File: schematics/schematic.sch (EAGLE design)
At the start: 22 parts, among them U1 TSR_1-2450

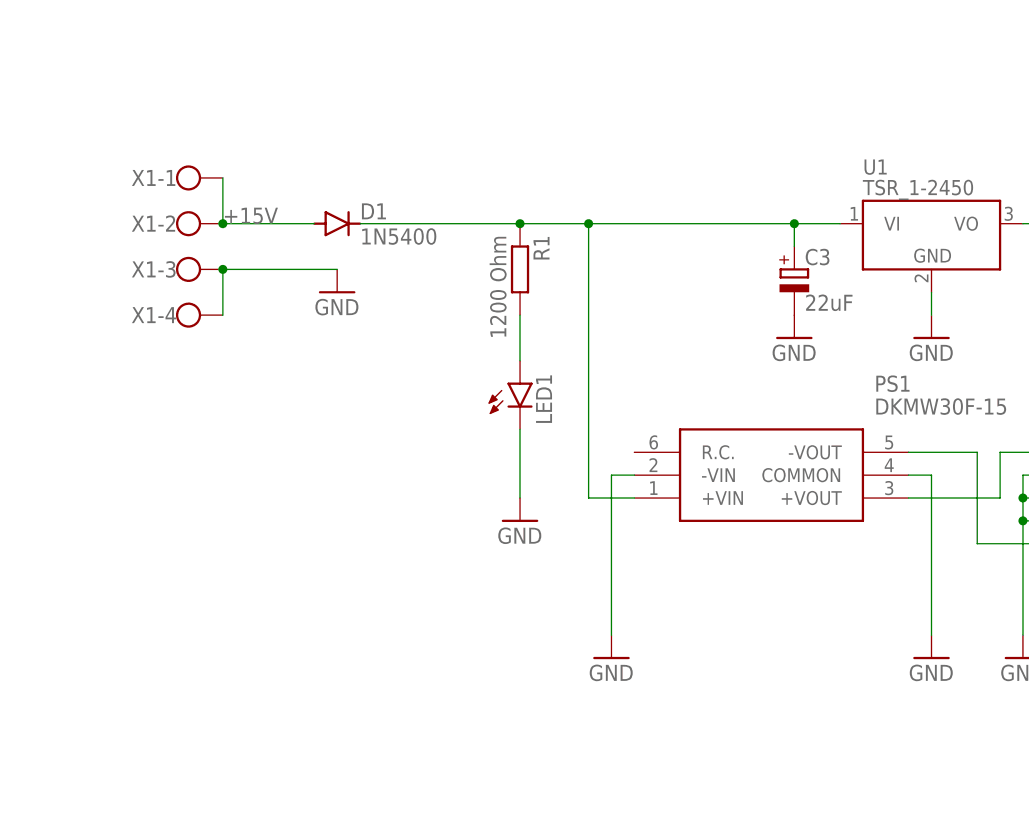
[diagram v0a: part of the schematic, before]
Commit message: added 2 crc groups
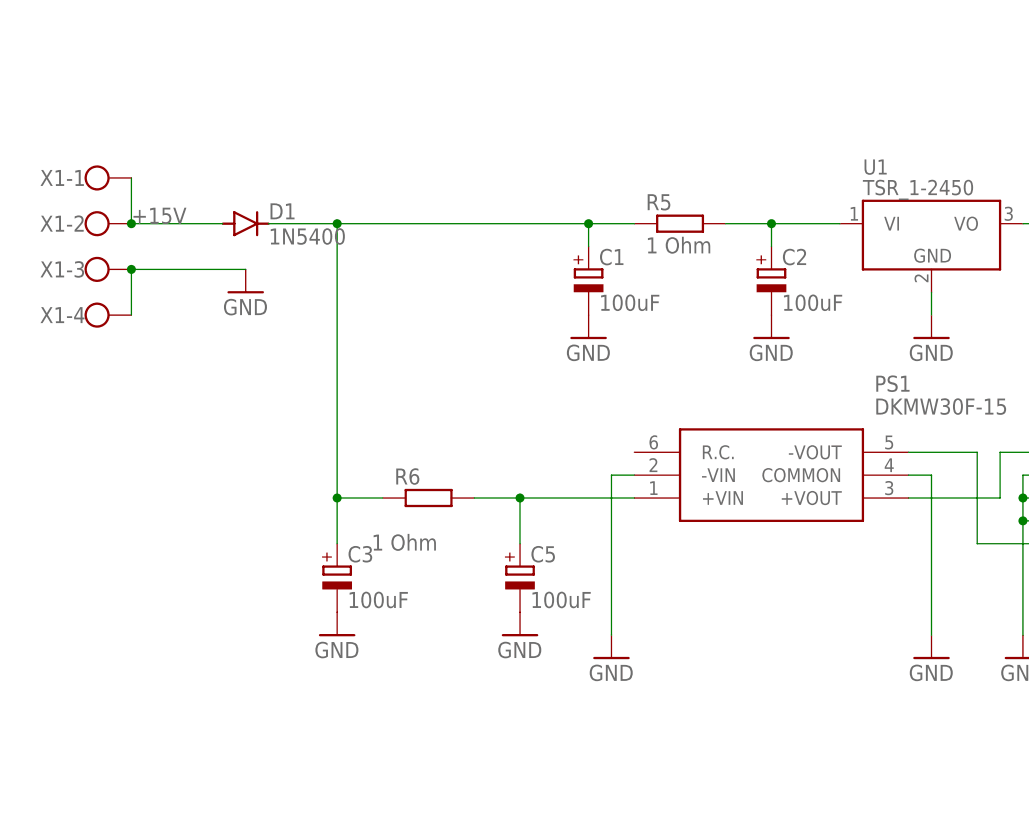
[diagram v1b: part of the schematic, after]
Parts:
- removed LED1: (no value), led:LED3MM
- removed R1: 1200 Ohm, rcl:R-EU_0207/10
- added C1, C2, C5: 100uF, rcl:CPOL-EUE3.5-8
- added R5, R6: 1 Ohm, rcl:R-EU_0207/10
- C3: value 22uF -> 100uF; device rcl:CPOL-EUE2.5-5 -> rcl:CPOL-EUE3.5-8
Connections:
- removed net N$2: LED1.A, R1.2
- new net N$8: C1.+, C3.+, D1.C, R5.1, R6.1
- new net VI1: C5.+, PS1.+VIN, R6.2
- net GND: now also C1.-, C2.-, C5.-; no longer LED1.C
- net VI: now also C2.+, R5.2; no longer C3.+, D1.C, PS1.+VIN, R1.1
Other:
- moved on the sheet: C3, D1, X1-1, X1-2, X1-3, X1-4

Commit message: bugfixes
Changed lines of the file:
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@@
 <instance part="R6" gate="G$1" x="27.94" y="66.04" smashed="yes">
 <attribute name="NAME" x="24.13" y="67.5386" size="1.778" layer="95"/>
-<attribute name="VALUE" x="21.59" y="60.198" size="1.778" layer="96"/>
+<attribute name="VALUE" x="24.13" y="62.738" size="1.778" layer="96"/>
 </instance>
 <instance part="C2" gate="G$1" x="66.04" y="91.44" smashed="yes">

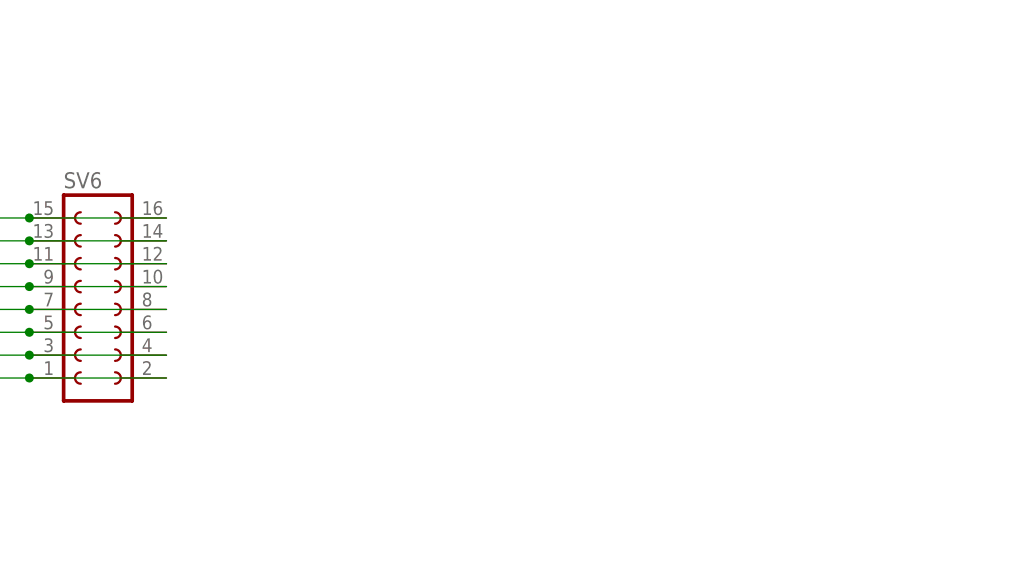
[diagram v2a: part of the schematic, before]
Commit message: added 4 more headers to board
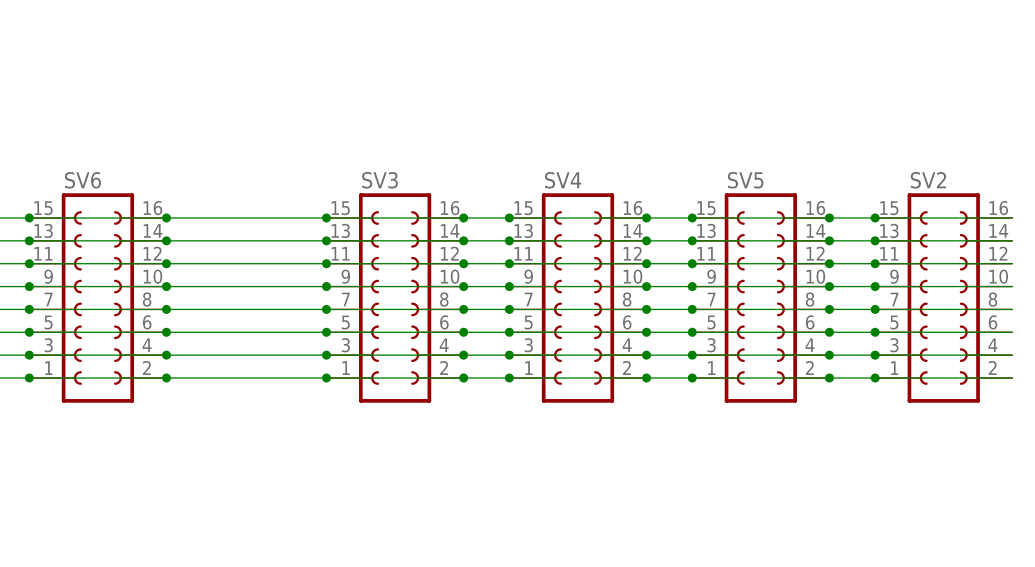
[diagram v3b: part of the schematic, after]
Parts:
- added SV2, SV3, SV4, SV5: (no value), con-lsta:FE08-2
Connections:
- net +12V: now also SV2.10, SV2.9, SV3.10, SV3.9, SV4.10, SV4.9, SV5.10, SV5.9
- net +5V: now also SV2.11, SV2.12, SV3.11, SV3.12, SV4.11, SV4.12, SV5.11, SV5.12
- net -12V: now also SV2.1, SV2.2, SV3.1, SV3.2, SV4.1, SV4.2, SV5.1, SV5.2
- net CV: now also SV2.13, SV2.14, SV3.13, SV3.14, SV4.13, SV4.14, SV5.13, SV5.14
- net GATE: now also SV2.15, SV2.16, SV3.15, SV3.16, SV4.15, SV4.16, SV5.15, SV5.16
- net GND: now also SV2.3, SV2.4, SV2.5, SV2.6, SV2.7, SV2.8, SV3.3, SV3.4, SV3.5, SV3.6, SV3.7, SV3.8, SV4.3, SV4.4, SV4.5, SV4.6, SV4.7, SV4.8, SV5.3, SV5.4, SV5.5, SV5.6, SV5.7, SV5.8
